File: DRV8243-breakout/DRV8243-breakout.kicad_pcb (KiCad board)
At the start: 2 copper layers, 40 x 40 mm, 20 parts, among them J1 Vin, J2 Motor_Output, J3 MCU_Connection, Q1 PMOS, U1 PDRV8243HRXYQ1

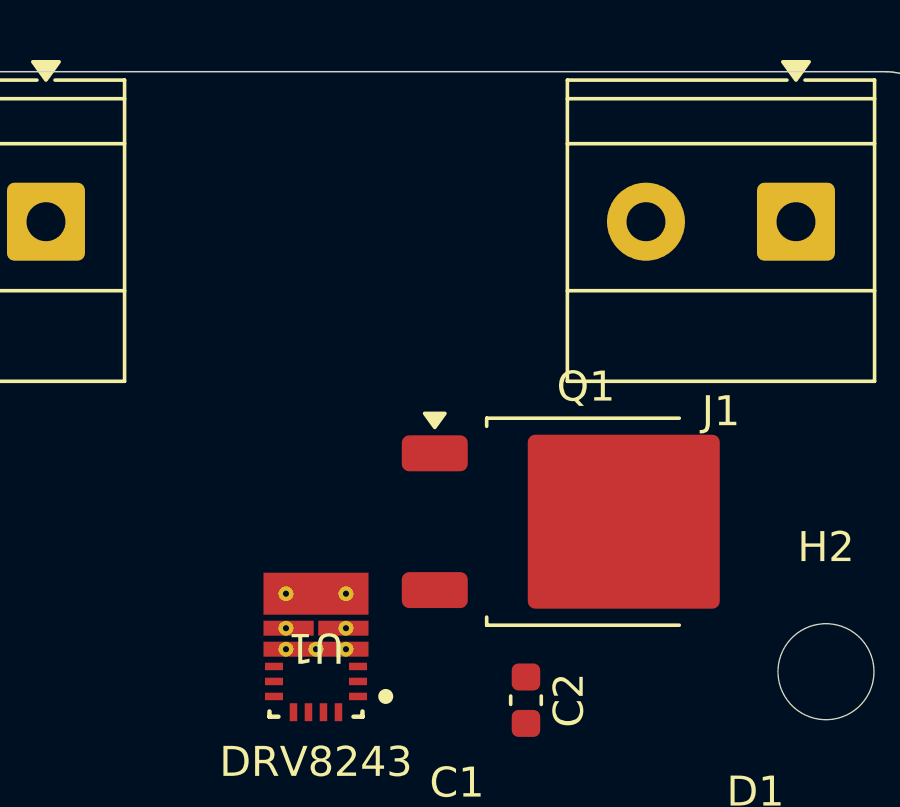
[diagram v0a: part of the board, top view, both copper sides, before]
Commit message: Update DRV8243-breakout.kicad_pcb
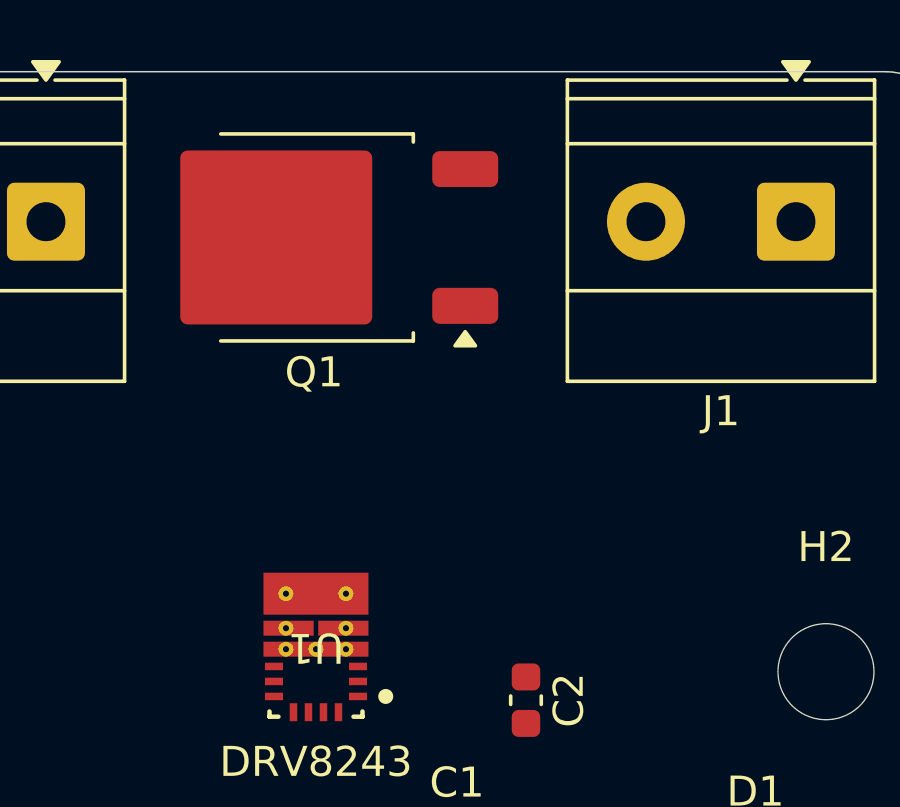
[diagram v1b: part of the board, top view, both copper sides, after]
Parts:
- moved Q1 13.1 mm to (168.9, 75.5), turned to 180 degrees
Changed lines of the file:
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@@
 	(footprint "Package_TO_SOT_SMD:TO-252-2"
 		(layer "F.Cu")
-		(at 178 85)
+		(at 168.935 75.525 180)
 		(descr "TO-252/DPAK SMD package, http://www.infineon.com/cms/en/product/packages/PG-TO252/PG-TO252-3-1/")
 		(tags "DPAK TO-252 DPAK-3 TO-252-3 SOT-428")
@@
 		)
 		(property "Sim.Device" "PMOS"
-			(at 0 0 0)
+			(at 0 0 180)
 			(unlocked yes)
 			(layer "F.Fab")
@@
 		)
 		(property "Sim.Type" "VDMOS"
-			(at 0 0 0)
+			(at 0 0 180)
 			(unlocked yes)
 			(layer "F.Fab")
@@
 		)
 		(property "Sim.Pins" "1=D 2=G 3=S"
-			(at 0 0 0)
+			(at 0 0 180)
 			(unlocked yes)
 			(layer "F.Fab")
@@
 		(attr smd)
 		(fp_line
+			(start 3.11 3.45)
+			(end -3.31 3.45)
+			(stroke
+				(width 0.12)
+				(type solid)
+			)
+			(layer "F.SilkS")
+		)
+		(fp_line
+			(start 3.11 -3.45)
+			(end -3.31 -3.45)
+			(stroke
+				(width 0.12)
+				(type solid)
+			)
+			(layer "F.SilkS")
+		)
+		(fp_line
+			(start -3.31 3.45)
+			(end -3.31 3.18)
+			(stroke
+				(width 0.12)
+				(type solid)
+			)
+			(layer "F.SilkS")
+		)
+		(fp_line
 			(start -3.31 -3.45)
 			(end -3.31 -3.18)
-			(stroke
-				(width 0.12)
-				(type solid)
-			)
-			(layer "F.SilkS")
-		)
-		(fp_line
-			(start -3.31 3.45)
-			(end -3.31 3.18)
-			(stroke
-				(width 0.12)
-				(type solid)
-			)
-			(layer "F.SilkS")
-		)
-		(fp_line
-			(start 3.11 -3.45)
-			(end -3.31 -3.45)
-			(stroke
-				(width 0.12)
-				(type solid)
-			)
-			(layer "F.SilkS")
-		)
-		(fp_line
-			(start 3.11 3.45)
-			(end -3.31 3.45)
 			(stroke
 				(width 0.12)
@@
 		)
 		(fp_line
+			(start 4.11 2.7)
+			(end 3.11 2.7)
+			(stroke
+				(width 0.1)
+				(type solid)
+			)
+			(layer "F.Fab")
+		)
+		(fp_line
+			(start 4.11 -2.7)
+			(end 4.11 2.7)
+			(stroke
+				(width 0.1)
+				(type solid)
+			)
+			(layer "F.Fab")
+		)
+		(fp_line
+			(start 3.11 -2.7)
+			(end 4.11 -2.7)
+			(stroke
+				(width 0.1)
+				(type solid)
+			)
+			(layer "F.Fab")
+		)
+		(fp_line
+			(start -2.705 -2.655)
+			(end -5.81 -2.655)
+			(stroke
+				(width 0.1)
+				(type solid)
+			)
+			(layer "F.Fab")
+		)
+		(fp_line
+			(start -3.11 1.905)
+			(end -5.81 1.905)
+			(stroke
+				(width 0.1)
+				(type solid)
+			)
+			(layer "F.Fab")
+		)
+		(fp_line
+			(start -5.81 2.655)
+			(end -3.11 2.655)
+			(stroke
+				(width 0.1)
+				(type solid)
+			)
+			(layer "F.Fab")
+		)
+		(fp_line
+			(start -5.81 1.905)
+			(end -5.81 2.655)
+			(stroke
+				(width 0.1)
+				(type solid)
+			)
+			(layer "F.Fab")
+		)
+		(fp_line
+			(start -5.81 -1.905)
+			(end -3.11 -1.905)
+			(stroke
+				(width 0.1)
+				(type solid)
+			)
+			(layer "F.Fab")
+		)
+		(fp_line
 			(start -5.81 -2.655)
 			(end -5.81 -1.905)
-			(stroke
-				(width 0.1)
-				(type solid)
-			)
-			(layer "F.Fab")
-		)
-		(fp_line
-			(start -5.81 -1.905)
-			(end -3.11 -1.905)
-			(stroke
-				(width 0.1)
-				(type solid)
-			)
-			(layer "F.Fab")
-		)
-		(fp_line
-			(start -5.81 1.905)
-			(end -5.81 2.655)
-			(stroke
-				(width 0.1)
-				(type solid)
-			)
-			(layer "F.Fab")
-		)
-		(fp_line
-			(start -5.81 2.655)
-			(end -3.11 2.655)
-			(stroke
-				(width 0.1)
-				(type solid)
-			)
-			(layer "F.Fab")
-		)
-		(fp_line
-			(start -3.11 1.905)
-			(end -5.81 1.905)
-			(stroke
-				(width 0.1)
-				(type solid)
-			)
-			(layer "F.Fab")
-		)
-		(fp_line
-			(start -2.705 -2.655)
-			(end -5.81 -2.655)
-			(stroke
-				(width 0.1)
-				(type solid)
-			)
-			(layer "F.Fab")
-		)
-		(fp_line
-			(start 3.11 -2.7)
-			(end 4.11 -2.7)
-			(stroke
-				(width 0.1)
-				(type solid)
-			)
-			(layer "F.Fab")
-		)
-		(fp_line
-			(start 4.11 -2.7)
-			(end 4.11 2.7)
-			(stroke
-				(width 0.1)
-				(type solid)
-			)
-			(layer "F.Fab")
-		)
-		(fp_line
-			(start 4.11 2.7)
-			(end 3.11 2.7)
 			(stroke
 				(width 0.1)
@@
 		)
 		(pad "" smd roundrect
-			(at -0.415 -1.525)
-			(size 3.05 2.75)
-			(layers "F.Paste")
-			(roundrect_rratio 0.090909)
-		)
-		(pad "" smd roundrect
-			(at -0.415 1.525)
-			(size 3.05 2.75)
-			(layers "F.Paste")
-			(roundrect_rratio 0.090909)
-		)
-		(pad "" smd roundrect
-			(at 2.935 -1.525)
-			(size 3.05 2.75)
-			(layers "F.Paste")
-			(roundrect_rratio 0.090909)
-		)
-		(pad "" smd roundrect
-			(at 2.935 1.525)
+			(at -0.415 -1.525 180)
+			(size 3.05 2.75)
+			(layers "F.Paste")
+			(roundrect_rratio 0.090909)
+		)
+		(pad "" smd roundrect
+			(at -0.415 1.525 180)
+			(size 3.05 2.75)
+			(layers "F.Paste")
+			(roundrect_rratio 0.090909)
+		)
+		(pad "" smd roundrect
+			(at 2.935 -1.525 180)
+			(size 3.05 2.75)
+			(layers "F.Paste")
+			(roundrect_rratio 0.090909)
+		)
+		(pad "" smd roundrect
+			(at 2.935 1.525 180)
 			(size 3.05 2.75)
 			(layers "F.Paste")
@@
 		)
 		(pad "1" smd roundrect
-			(at -5.04 -2.28)
+			(at -5.04 -2.28 180)
 			(size 2.2 1.2)
 			(layers "F.Cu" "F.Mask" "F.Paste")
@@
 		)
 		(pad "2" smd roundrect
-			(at 1.26 0)
+			(at 1.26 0 180)
 			(size 6.4 5.8)
 			(layers "F.Cu" "F.Mask")
@@
 		)
 		(pad "3" smd roundrect
-			(at -5.04 2.28)
+			(at -5.04 2.28 180)
 			(size 2.2 1.2)
 			(layers "F.Cu" "F.Mask" "F.Paste")

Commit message: Fix mosfet footprint
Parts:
- Q1: footprint Package_TO_SOT_SMD:TO-252-2 -> DRV8243:TO-252-2(DPAK)
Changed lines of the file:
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@@
 		)
 	)
-	(footprint "Package_TO_SOT_SMD:TO-252-2"
+	(footprint "DRV8243:TO-252-2(DPAK)"
 		(layer "F.Cu")
 		(at 168.935 75.525 180)
@@
 		(tags "DPAK TO-252 DPAK-3 TO-252-3 SOT-428")
 		(property "Reference" "Q1"
-			(at 0 -4.5 0)
+			(at 0 -4.5 180)
 			(layer "F.SilkS")
 			(effects
@@
 		)
 		(property "Value" "PMOS"
-			(at 0 4.5 0)
+			(at 0 4.5 180)
 			(layer "F.Fab")
 			(effects
@@
 		)
 		(property "Datasheet" "https://ngspice.sourceforge.io/docs/ngspice-html-manual/manual.xhtml#cha_MOSFETs"
-			(at 0 0 0)
+			(at 0 0 180)
 			(layer "F.Fab")
 			(hide yes)
@@
 		)
 		(property "Description" "P-MOSFET transistor, drain/source/gate"
-			(at 0 0 0)
+			(at 0 0 180)
 			(layer "F.Fab")
 			(hide yes)
@@
 		)
 		(fp_text user "${REFERENCE}"
-			(at 0 0 0)
+			(at 0 0 180)
 			(layer "F.Fab")
 			(effects
@@
 		)
 		(pad "1" smd roundrect
+			(at 1.26 0 180)
+			(size 6.4 5.8)
+			(layers "F.Cu" "F.Mask")
+			(roundrect_rratio 0.043103)
+			(net 6 "Net-(J1-Pin_2)")
+			(pinfunction "D")
+			(pintype "passive")
+		)
+		(pad "2" smd roundrect
 			(at -5.04 -2.28 180)
 			(size 2.2 1.2)
 			(layers "F.Cu" "F.Mask" "F.Paste")
 			(roundrect_rratio 0.208333)
-			(net 6 "Net-(J1-Pin_2)")
-			(pinfunction "D")
-			(pintype "passive")
-		)
-		(pad "2" smd roundrect
-			(at 1.26 0 180)
-			(size 6.4 5.8)
-			(layers "F.Cu" "F.Mask")
-			(roundrect_rratio 0.043103)
 			(net 4 "Net-(D1-A)")
 			(pinfunction "G")

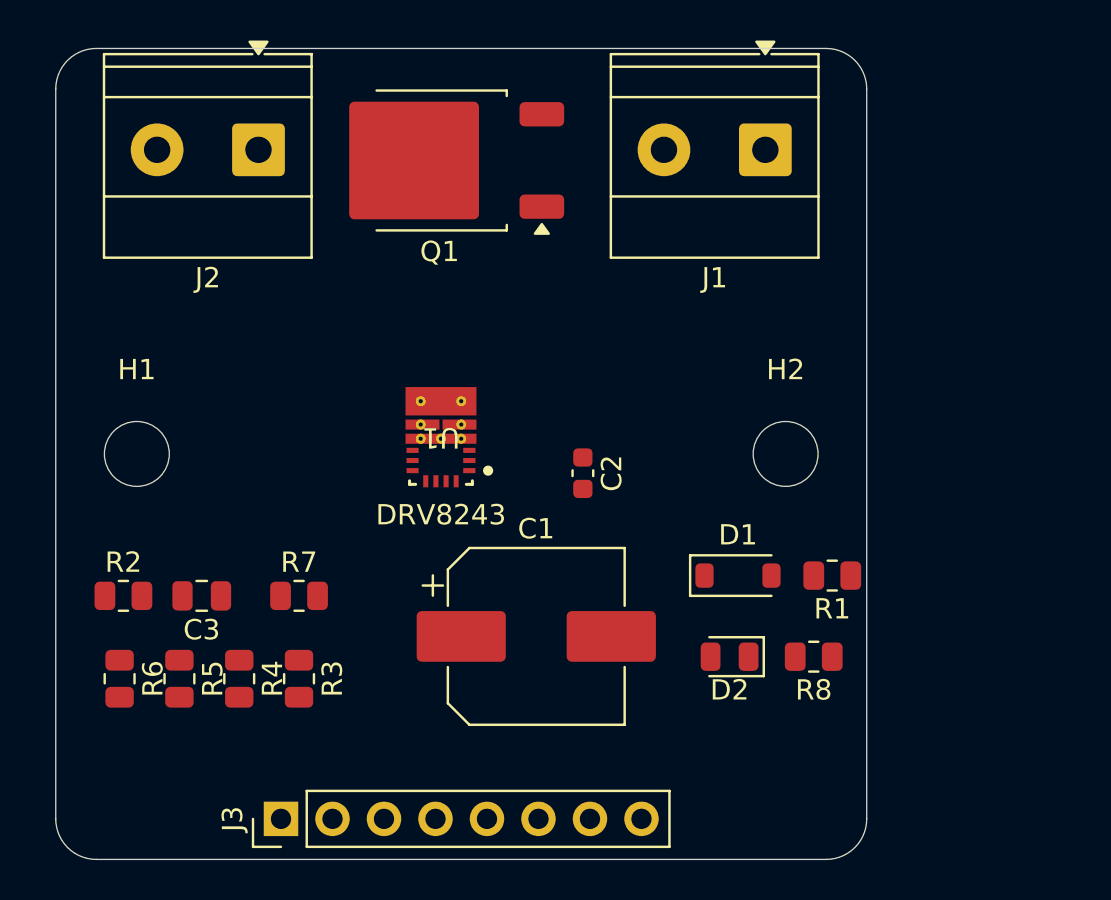
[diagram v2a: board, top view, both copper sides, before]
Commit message: Add second driver
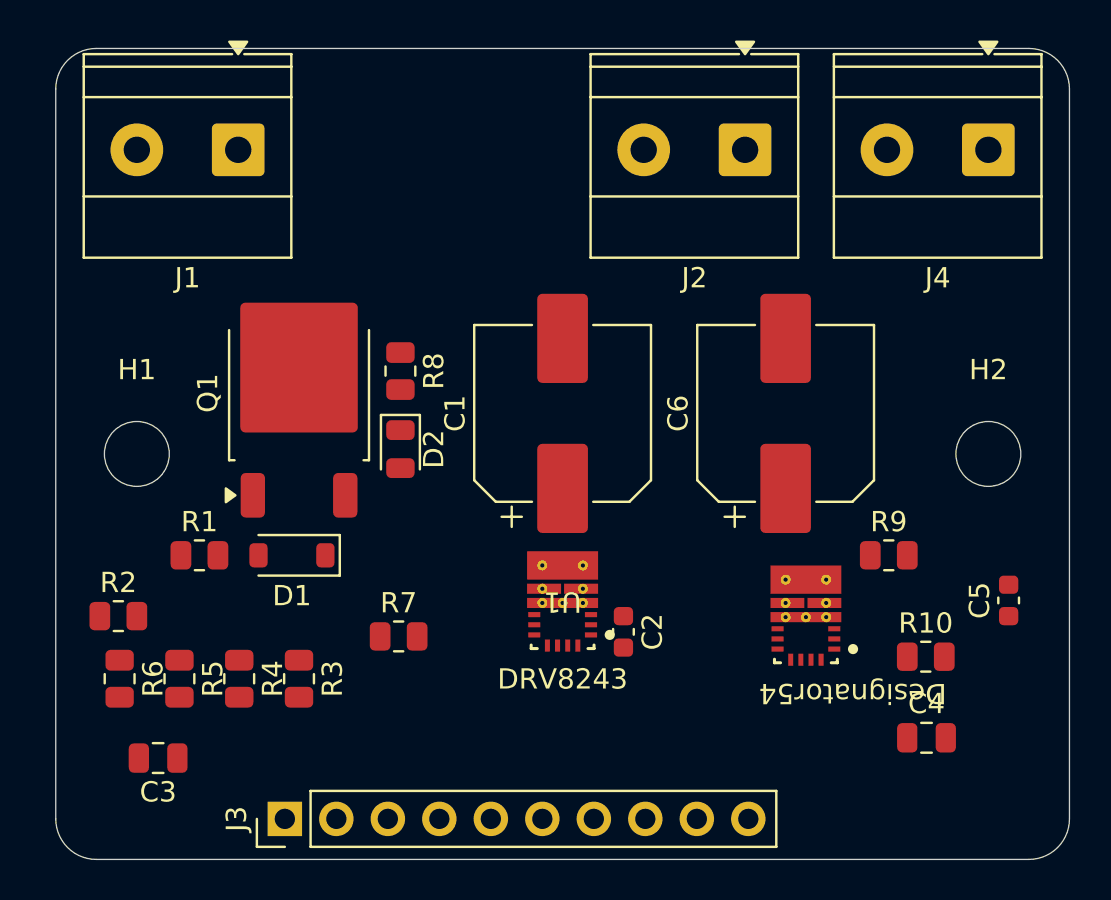
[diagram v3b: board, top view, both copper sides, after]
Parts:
- added C4: DNP, Capacitor_SMD:C_0805_2012Metric, F.Cu at (192.9, 104.0)
- added C5: 0.1uF, Capacitor_SMD:C_0603_1608Metric, F.Cu at (197.0, 97.2)
- added C6: 220uF, Capacitor_SMD:CP_Elec_8x10.5, F.Cu at (186.0, 88.0)
- added J4: Motor_Output, TerminalBlock_Phoenix:TerminalBlock_Phoenix_MKDS-1,5-2_1x02_P5.00mm_Horizontal, F.Cu at (196.0, 75.0)
- added R10: 820, Resistor_SMD:R_0805_2012Metric, F.Cu at (192.9, 100.0)
- added R9: 5k, Resistor_SMD:R_0805_2012Metric, F.Cu at (191.1, 95.0)
- added U2: PDRV8243HRXYQ1, DRV8243:RXY0014A-MFG, F.Cu at (187.0, 98.0)
- J3: value MCU_Connection -> Conn_01x10_Pin; footprint Connector_PinHeader_2.54mm:PinHeader_1x08_P2.54mm_Vertical -> Connector_PinHeader_2.54mm:PinHeader_1x10_P2.54mm_Vertical
- Q1: value PMOS -> PMOS-AOD409
- moved R1 31.2 mm to (157.1, 95.0), turned to 0 degrees
- moved J1 26.0 mm to (159.0, 75.0)
- moved R8 24.8 mm to (167.0, 85.9), turned to -90 degrees
- moved J2 24.0 mm to (184.0, 75.0)
- moved D1 22.0 mm to (161.7, 95.0), turned to 180 degrees
- moved D2 19.2 mm to (167.0, 89.8), turned to -90 degrees
- moved Q1 13.4 mm to (162.0, 87.0), turned to 90 degrees
- moved C1 11.1 mm to (175.0, 88.0), turned to 90 degrees
- moved U1 10.1 mm to (175.0, 97.3)
- moved H2 10.0 mm to (196.0, 90.0)
- moved C3 8.28 mm to (155.1, 105.0)
- moved C2 8.08 mm to (178.0, 98.8)
- moved R7 5.30 mm to (166.9, 99.0)
- moved R2 1.03 mm to (153.1, 98.0)
- moved J3 0.19 mm to (161.3, 108.0)
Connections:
- net Net-(J1-Pin_2) renamed /Vin
- J3 pad 7: IPROPI -> IN3
- J3 pad 8: nFault -> IN4
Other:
- board size 40 x 40 mm -> 50 x 40 mm

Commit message: layout updates
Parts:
- J3: value Conn_01x10_Pin -> Conn_01x11_Pin; footprint Connector_PinHeader_2.54mm:PinHeader_1x10_P2.54mm_Vertical -> Connector_PinHeader_2.54mm:PinHeader_1x11_P2.54mm_Vertical
- moved R2 29.1 mm to (181.9, 102.0), turned to -90 degrees
- moved C3 24.6 mm to (179.5, 102.0), turned to -90 degrees
- moved R7 10.5 mm to (177.0, 101.9), turned to 90 degrees
- moved R9 7.67 mm to (190.0, 102.6), turned to 90 degrees
- moved R6 7.19 mm to (156.4, 107.5), turned to 0 degrees
- moved C5 6.52 mm to (190.5, 96.8)
- moved R3 6.10 mm to (156.4, 98.7), turned to 0 degrees
- moved R5 3.48 mm to (156.4, 104.5), turned to 0 degrees
- moved R4 2.69 mm to (156.4, 101.6), turned to 0 degrees
- moved R10 2.65 mm to (194.0, 102.4), turned to -90 degrees
- moved C2 2.05 mm to (178.0, 96.7), turned to 90 degrees
- moved J3 2.04 mm to (163.3, 108.0)
- moved C4 1.82 mm to (192.0, 102.5), turned to -90 degrees
- moved C6 1.51 mm to (187.5, 88.2)
- moved U2 0.54 mm to (187.5, 97.8)
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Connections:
- C3 pad 1: IPROPI -> IPROPI0
- C4 pad 1: IPROPI -> IPROPI1
- J3 pad 10: nFault -> IPROPI1
- J3 pad 9: IPROPI -> IPROPI0
- R10 pad 1: IPROPI -> IPROPI1
- R2 pad 1: IPROPI -> IPROPI0
- U1 pad 2: IPROPI -> IPROPI0
- U2 pad 2: IPROPI -> IPROPI1

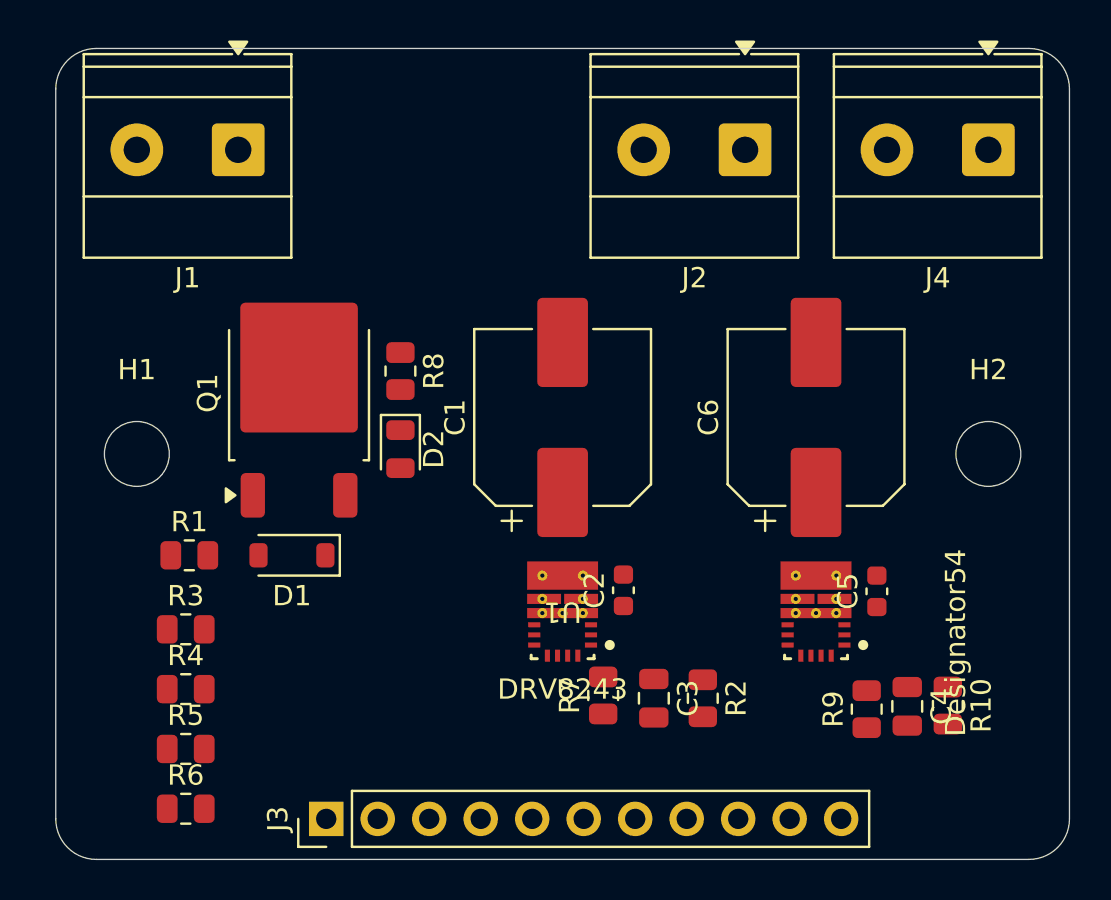
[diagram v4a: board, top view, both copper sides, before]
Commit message: Create netclasses and begin routing
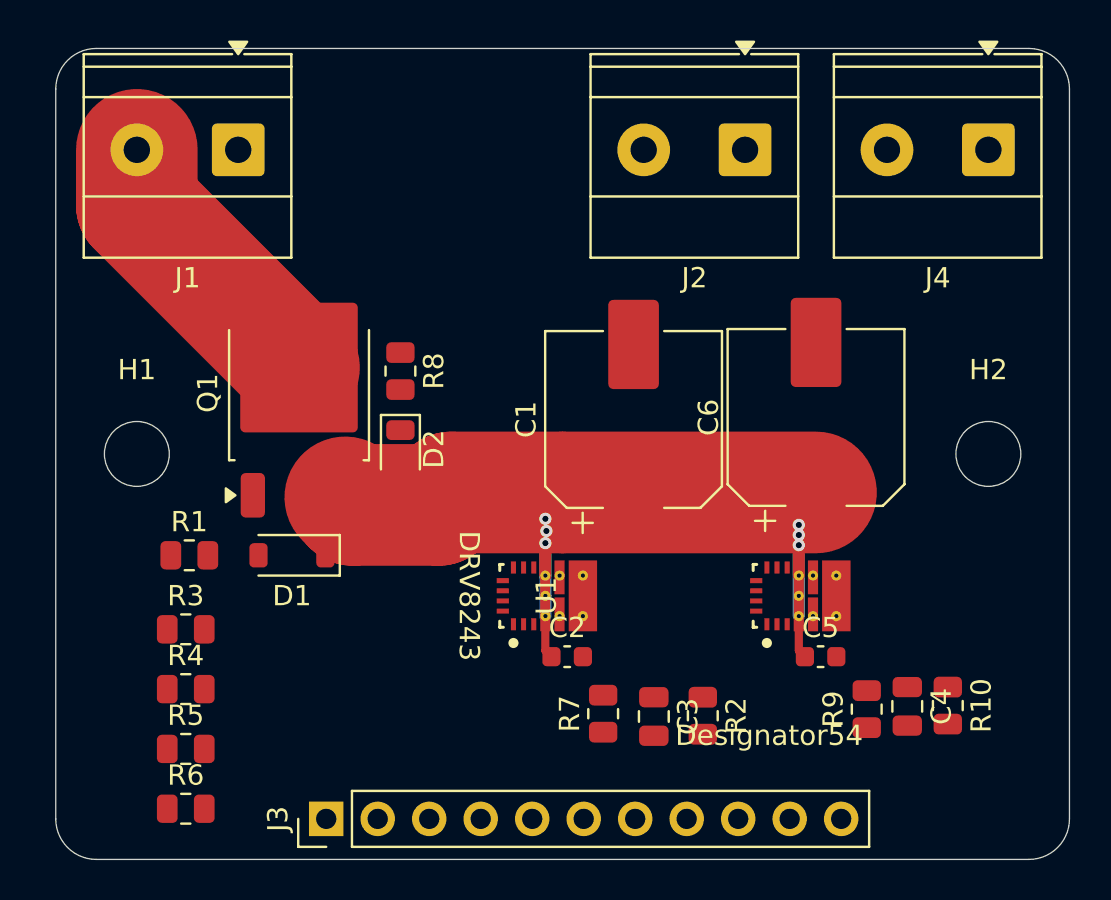
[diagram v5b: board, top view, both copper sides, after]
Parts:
- moved C2 4.29 mm to (175.2, 100.0), turned to 0 degrees
- moved C5 4.25 mm to (187.7, 100.0), turned to 0 degrees
- moved C1 3.50 mm to (178.5, 88.3)
- moved U2 1.13 mm to (186.7, 97.0), turned to 90 degrees
- moved U1 1.13 mm to (174.2, 97.0), turned to 90 degrees
- moved C3 0.90 mm to (179.5, 103.0)
- moved R7 0.90 mm to (177.0, 102.8)
- moved R2 0.86 mm to (181.9, 102.9)
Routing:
- net VM: track 0.00 -> 44.8 mm, vias 0 -> 6
- net /Vin: track 0.00 -> 14.1 mm
